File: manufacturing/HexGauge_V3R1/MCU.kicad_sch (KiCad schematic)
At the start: 26 parts, among them SW2 SW_Omron_B3FS, SW2 SW_SPDT, U2 STM32F405RGT6, Y1 25MHz 12pF

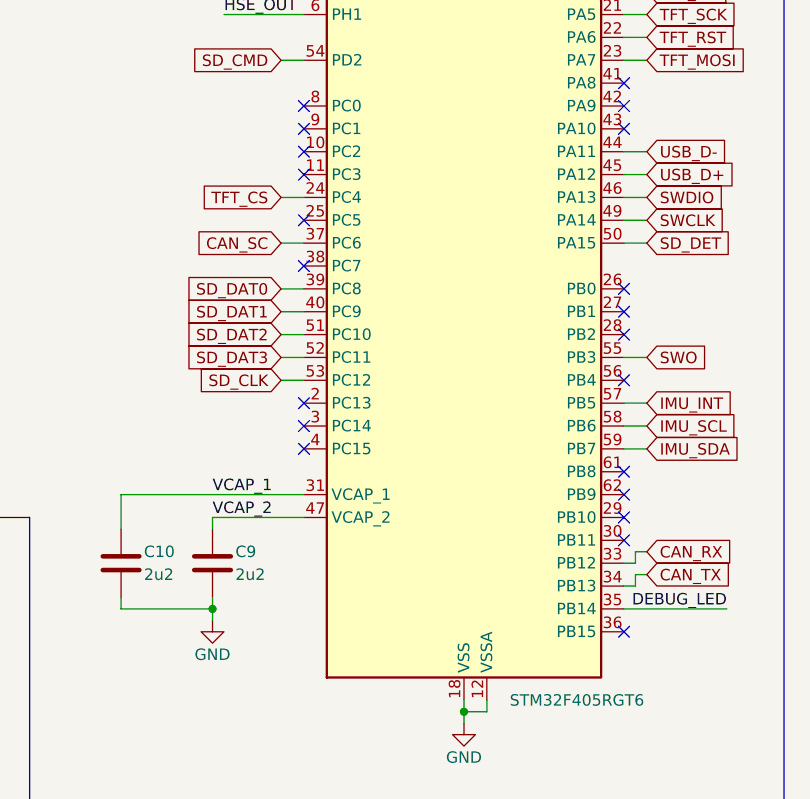
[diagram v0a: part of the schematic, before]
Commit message: Updated Component Selection
Better availability
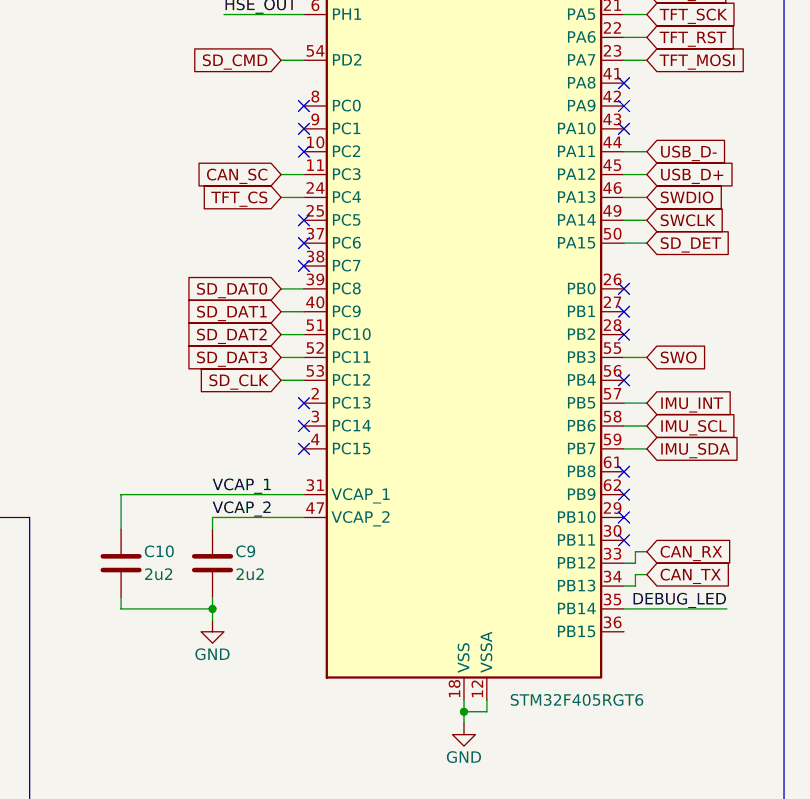
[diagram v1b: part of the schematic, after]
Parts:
- D1: LCSC Part # (none) -> C2290
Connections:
- net CAN_SC: now also U2.11 (PC3); no longer U2.37 (PC6)
- no-connect marks 24 -> 23
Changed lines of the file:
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@@
   (no_connect (at 121.92 113.03))
   (no_connect (at 86.36 95.25))
-  (no_connect (at 86.36 100.33))
+  (no_connect (at 86.36 107.95))
   (no_connect (at 121.92 115.57))
   (no_connect (at 86.36 110.49))
@@
   (no_connect (at 121.92 90.17))
   (no_connect (at 121.92 133.35))
-  (no_connect (at 121.92 151.13))
   (no_connect (at 86.36 105.41))
   (wire (pts (xy 124.46 80.01) (xy 121.92 80.01))
@@
     (stroke (width 0) (type default))
   )
+  (wire (pts (xy 83.82 100.33) (xy 86.36 100.33))
+    (stroke (width 0) (type default))
+  )
   (wire (pts (xy 78.74 59.69) (xy 67.31 59.69))
     (stroke (width 0) (type default))
@@
   )
   (wire (pts (xy 45.72 59.69) (xy 34.29 59.69))
-    (stroke (width 0) (type default))
-  )
-  (wire (pts (xy 83.82 107.95) (xy 86.36 107.95))
     (stroke (width 0) (type default))
   )
@@
     )
   )
+  (global_label "CAN_SC" (shape input) (at 83.82 100.33 180) (fields_autoplaced)
+    (effects (font (size 1.27 1.27)) (justify right))
+    (property "Intersheetrefs" "${INTERSHEET_REFS}" (at 73.778 100.33 0)
+      (effects (font (size 1.27 1.27)) (justify right) hide)
+    )
+  )
   (global_label "NRST" (shape input) (at 83.82 69.85 180) (fields_autoplaced)
     (effects (font (size 1.27 1.27)) (justify right))
     (property "Intersheetrefs" "${INTERSHEET_REFS}" (at 76.1366 69.85 0)
-      (effects (font (size 1.27 1.27)) (justify right) hide)
-    )
-  )
-  (global_label "CAN_SC" (shape input) (at 83.82 107.95 180) (fields_autoplaced)
-    (effects (font (size 1.27 1.27)) (justify right))
-    (property "Intersheetrefs" "${INTERSHEET_REFS}" (at 73.778 107.95 0)
       (effects (font (size 1.27 1.27)) (justify right) hide)
     )
@@
       (effects (font (size 1.27 1.27)) hide)
     )
+    (property "LCSC Part #" "C2290" (at 223.52 115.57 0)
+      (effects (font (size 1.27 1.27)) hide)
+    )

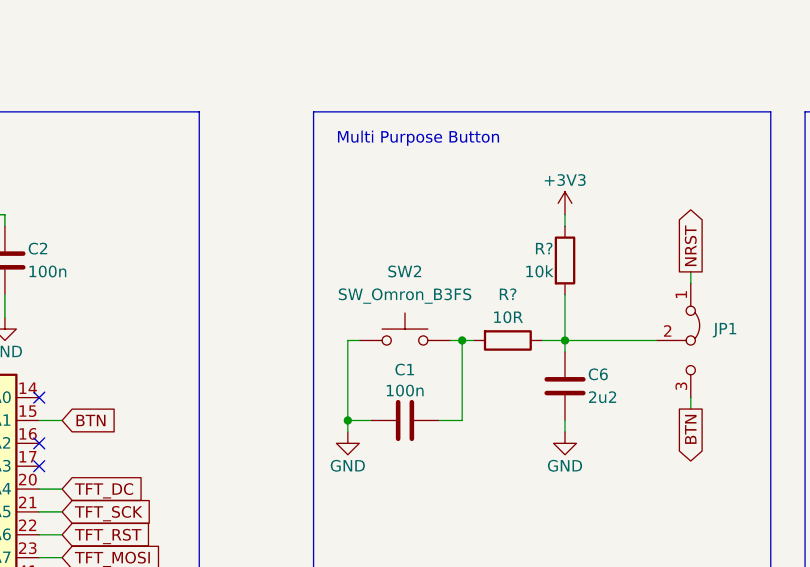
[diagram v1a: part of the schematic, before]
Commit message: Cost calculation
Find extended parts on mouser
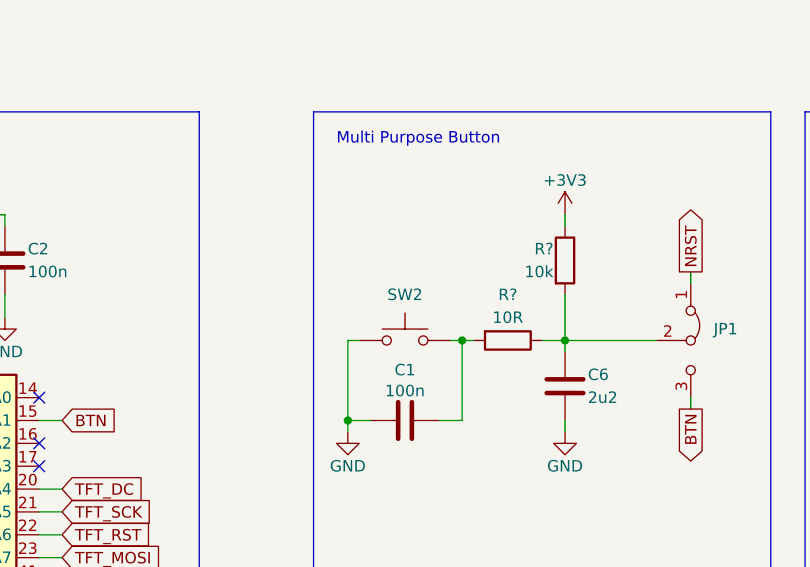
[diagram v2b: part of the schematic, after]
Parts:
- SW2: LCSC Part # (none) -> C221841
- SW2: value SW_Omron_B3FS -> SW_Panasonic_EVQPUC; LCSC Part # (none) -> C79174
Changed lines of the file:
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@@
       (effects (font (size 1.27 1.27)) hide)
     )
-    (property "Datasheet" "~" (at 220.98 66.04 0)
+    (property "Datasheet" "https://datasheet.lcsc.com/lcsc/1912111437_C-K-PCM12SMTR_C221841.pdf" (at 220.98 66.04 0)
+      (effects (font (size 1.27 1.27)) hide)
+    )
+    (property "LCSC Part #" "C221841" (at 220.98 66.04 0)
       (effects (font (size 1.27 1.27)) hide)
     )
@@
   (symbol (lib_id "Switch:SW_Omron_B3FS") (at 162.56 63.5 0) (unit 1)
     (in_bom yes) (on_board yes) (dnp no) (fields_autoplaced)
-    (property "Reference" "SW2" (at 162.56 55.88 0)
+    (property "Reference" "SW2" (at 162.56 58.42 0)
       (effects (font (size 1.27 1.27)))
     )
-    (property "Value" "SW_Omron_B3FS" (at 162.56 58.42 0)
-      (effects (font (size 1.27 1.27)))
+    (property "Value" "SW_Panasonic_EVQPUC" (at 162.56 58.42 0)
+      (effects (font (size 1.27 1.27)) hide)
     )
     (property "Footprint" "Button_Switch_SMD:Panasonic_EVQPUL_EVQPUC" (at 162.56 58.42 0)
       (effects (font (size 1.27 1.27)) hide)
     )
-    (property "Datasheet" "https://omronfs.omron.com/en_US/ecb/products/pdf/en-b3fs.pdf" (at 162.56 58.42 0)
+    (property "Datasheet" "https://datasheet.lcsc.com/lcsc/2304140030_PANASONIC-EVQPUC02K_C79174.pdf" (at 162.56 58.42 0)
       (effects (font (size 1.27 1.27)) hide)
     )
+    (property "LCSC Part #" "C79174" (at 162.56 63.5 0)
+      (effects (font (size 1.27 1.27)) hide)
+    )
